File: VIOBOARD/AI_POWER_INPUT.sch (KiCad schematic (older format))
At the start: 17 parts, among them J6 SENSOR INPUT

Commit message: Libraries modified as part of the BBB cape developement.
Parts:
- D13, D14, D15, D16, D17, D18, D19, D4: symbol device:D_Schottky_x2_Serial_AKC -> VIOBOARD-rescue:D_Schottky_x2_Serial_AKC-device
- R53, R54, R55, R56, R57, R58, R59, R60: symbol device:R -> VIOBOARD-rescue:R-device
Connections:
- wire segments 27 -> 49
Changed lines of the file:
@@
 $EndComp
 Wire Wire Line
-	4800 1550 10350 1550
-Wire Wire Line
-	4800 2950 10350 2950
-Wire Wire Line
-	4800 2750 10350 2750
-Wire Wire Line
-	4800 2550 10350 2550
-Wire Wire Line
-	4800 2350 10350 2350
-Wire Wire Line
-	4800 2150 10350 2150
-Wire Wire Line
-	4800 1950 10350 1950
+	4800 1550 9450 1550
+Wire Wire Line
+	4800 2950 6300 2950
+Wire Wire Line
+	4800 2750 6750 2750
+Wire Wire Line
+	4800 2550 7200 2550
+Wire Wire Line
+	4800 2350 7650 2350
+Wire Wire Line
+	4800 2150 8100 2150
+Wire Wire Line
+	4800 1950 8550 1950
 Text Notes 7300 650  0    60   ~ 0
 BOM - 2017-06-09
 $Comp
-L device:D_Schottky_x2_Serial_AKC D4
+L VIOBOARD-rescue:D_Schottky_x2_Serial_AKC-device D4
 U 1 1 599A54A1
 P 6100 3800
@@
 $EndComp
 $Comp
-L device:D_Schottky_x2_Serial_AKC D13
+L VIOBOARD-rescue:D_Schottky_x2_Serial_AKC-device D13
 U 1 1 599A8435
 P 6550 3800
@@
 $EndComp
 $Comp
-L device:D_Schottky_x2_Serial_AKC D14
+L VIOBOARD-rescue:D_Schottky_x2_Serial_AKC-device D14
 U 1 1 599A8476
 P 7000 3800
@@
 $EndComp
 $Comp
-L device:D_Schottky_x2_Serial_AKC D15
+L VIOBOARD-rescue:D_Schottky_x2_Serial_AKC-device D15
 U 1 1 599A84BE
 P 7450 3800
@@
 $EndComp
 $Comp
-L device:D_Schottky_x2_Serial_AKC D16
+L VIOBOARD-rescue:D_Schottky_x2_Serial_AKC-device D16
 U 1 1 599A8509
 P 7900 3800
@@
 $EndComp
 $Comp
-L device:D_Schottky_x2_Serial_AKC D17
+L VIOBOARD-rescue:D_Schottky_x2_Serial_AKC-device D17
 U 1 1 599A8571
 P 8350 3800
@@
 $EndComp
 $Comp
-L device:D_Schottky_x2_Serial_AKC D18
+L VIOBOARD-rescue:D_Schottky_x2_Serial_AKC-device D18
 U 1 1 599A85C6
 P 8800 3800
@@
 $EndComp
 $Comp
-L device:D_Schottky_x2_Serial_AKC D19
+L VIOBOARD-rescue:D_Schottky_x2_Serial_AKC-device D19
 U 1 1 599A861A
 P 9250 3800
@@
 $EndComp
 Wire Wire Line
-	5600 4100 9250 4100
+	5600 4100 6100 4100
 Connection ~ 8800 4100
 Connection ~ 8350 4100
@@
 $EndComp
 Wire Wire Line
-	4850 3500 9250 3500
+	4850 3500 6100 3500
 Connection ~ 8800 3500
 Connection ~ 8350 3500
@@
 Connection ~ 9450 1550
 Wire Wire Line
-	4800 1750 10350 1750
+	4800 1750 9000 1750
 Connection ~ 9000 1750
 $Comp
-L device:R R53
+L VIOBOARD-rescue:R-device R53
 U 1 1 5A414C98
 P 6300 3200
@@
 $EndComp
 $Comp
-L device:R R54
+L VIOBOARD-rescue:R-device R54
 U 1 1 5A414CD7
 P 6750 3200
@@
 $EndComp
 $Comp
-L device:R R55
+L VIOBOARD-rescue:R-device R55
 U 1 1 5A414D22
 P 7200 3200
@@
 $EndComp
 $Comp
-L device:R R56
+L VIOBOARD-rescue:R-device R56
 U 1 1 5A414D6F
 P 7650 3200
@@
 $EndComp
 $Comp
-L device:R R57
+L VIOBOARD-rescue:R-device R57
 U 1 1 5A414DB4
 P 8100 3200
@@
 $EndComp
 $Comp
-L device:R R58
+L VIOBOARD-rescue:R-device R58
 U 1 1 5A414DF5
 P 8550 3200
@@
 $EndComp
 $Comp
-L device:R R59
+L VIOBOARD-rescue:R-device R59
 U 1 1 5A414E50
 P 9000 3200
@@
 $EndComp
 $Comp
-L device:R R60
+L VIOBOARD-rescue:R-device R60
 U 1 1 5A414EAD
 P 9450 3200
@@
 Wire Wire Line
 	6300 3350 6300 3800
+Wire Wire Line
+	8800 4100 9250 4100
+Wire Wire Line
+	8350 4100 8800 4100
+Wire Wire Line
+	7900 4100 8350 4100
+Wire Wire Line
+	7450 4100 7900 4100
+Wire Wire Line
+	7000 4100 7450 4100
+Wire Wire Line
+	6550 4100 7000 4100
+Wire Wire Line
+	6100 4100 6550 4100
+Wire Wire Line
+	8800 3500 9250 3500
+Wire Wire Line
+	8350 3500 8800 3500
+Wire Wire Line
+	7900 3500 8350 3500
+Wire Wire Line
+	7450 3500 7900 3500
+Wire Wire Line
+	7000 3500 7450 3500
+Wire Wire Line
+	6550 3500 7000 3500
+Wire Wire Line
+	6100 3500 6550 3500
+Wire Wire Line
+	6300 2950 10350 2950
+Wire Wire Line
+	6750 2750 10350 2750
+Wire Wire Line
+	7200 2550 10350 2550
+Wire Wire Line
+	7650 2350 10350 2350
+Wire Wire Line
+	8100 2150 10350 2150
+Wire Wire Line
+	8550 1950 10350 1950
+Wire Wire Line
+	9450 1550 10350 1550
+Wire Wire Line
+	9000 1750 10350 1750
 $EndSCHEMATC

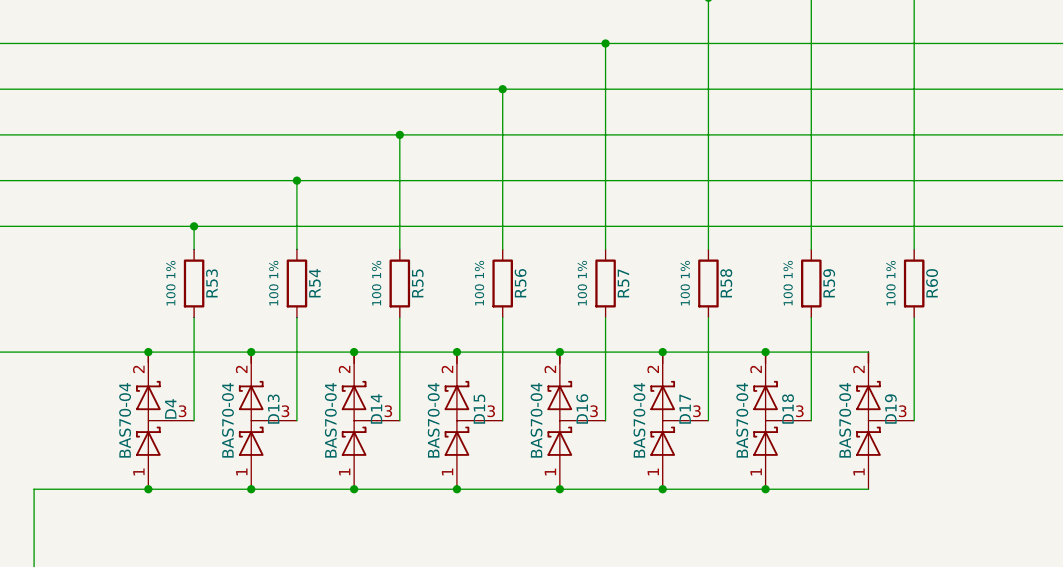
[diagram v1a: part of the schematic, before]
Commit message: Schematics cleanup.  Gerbers for the latest manufacturing release.
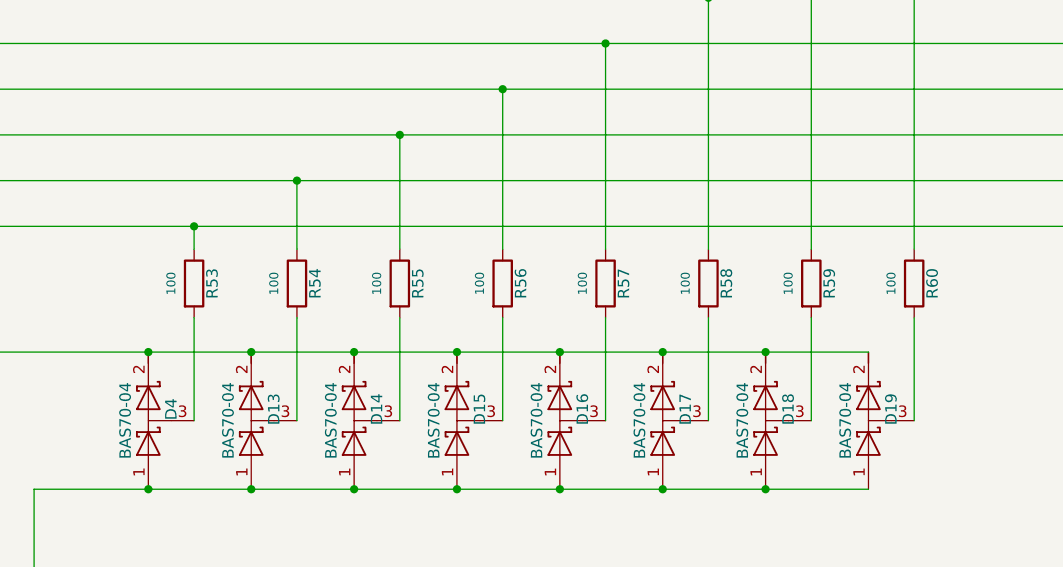
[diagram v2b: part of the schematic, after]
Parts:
- R53, R54, R55, R56, R57, R58, R59, R60: value 100 1% -> 100
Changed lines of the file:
@@
 P 6300 3200
 F 0 "R53" V 6380 3200 50  0000 C CNN
-F 1 "100 1%" V 6200 3200 39  0000 C CNN
+F 1 "100" V 6200 3200 39  0000 C CNN
 F 2 "Resistors_SMD:R_0805" V 6230 3200 50  0001 C CNN
 F 3 "" H 6300 3200 50  0001 C CNN
@@
 P 6750 3200
 F 0 "R54" V 6830 3200 50  0000 C CNN
-F 1 "100 1%" V 6650 3200 39  0000 C CNN
+F 1 "100" V 6650 3200 39  0000 C CNN
 F 2 "Resistors_SMD:R_0805" V 6680 3200 50  0001 C CNN
 F 3 "" H 6750 3200 50  0001 C CNN
@@
 P 7200 3200
 F 0 "R55" V 7280 3200 50  0000 C CNN
-F 1 "100 1%" V 7100 3200 39  0000 C CNN
+F 1 "100" V 7100 3200 39  0000 C CNN
 F 2 "Resistors_SMD:R_0805" V 7130 3200 50  0001 C CNN
 F 3 "" H 7200 3200 50  0001 C CNN
@@
 P 7650 3200
 F 0 "R56" V 7730 3200 50  0000 C CNN
-F 1 "100 1%" V 7550 3200 39  0000 C CNN
+F 1 "100" V 7550 3200 39  0000 C CNN
 F 2 "Resistors_SMD:R_0805" V 7580 3200 50  0001 C CNN
 F 3 "" H 7650 3200 50  0001 C CNN
@@
 P 8100 3200
 F 0 "R57" V 8180 3200 50  0000 C CNN
-F 1 "100 1%" V 8000 3200 39  0000 C CNN
+F 1 "100" V 8000 3200 39  0000 C CNN
 F 2 "Resistors_SMD:R_0805" V 8030 3200 50  0001 C CNN
 F 3 "" H 8100 3200 50  0001 C CNN
@@
 P 8550 3200
 F 0 "R58" V 8630 3200 50  0000 C CNN
-F 1 "100 1%" V 8450 3200 39  0000 C CNN
+F 1 "100" V 8450 3200 39  0000 C CNN
 F 2 "Resistors_SMD:R_0805" V 8480 3200 50  0001 C CNN
 F 3 "" H 8550 3200 50  0001 C CNN
@@
 P 9000 3200
 F 0 "R59" V 9080 3200 50  0000 C CNN
-F 1 "100 1%" V 8900 3200 39  0000 C CNN
+F 1 "100" V 8900 3200 39  0000 C CNN
 F 2 "Resistors_SMD:R_0805" V 8930 3200 50  0001 C CNN
 F 3 "" H 9000 3200 50  0001 C CNN
@@
 P 9450 3200
 F 0 "R60" V 9530 3200 50  0000 C CNN
-F 1 "100 1%" V 9350 3200 39  0000 C CNN
+F 1 "100" V 9350 3200 39  0000 C CNN
 F 2 "Resistors_SMD:R_0805" V 9380 3200 50  0001 C CNN
 F 3 "" H 9450 3200 50  0001 C CNN
